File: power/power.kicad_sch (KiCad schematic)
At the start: 160 parts, among them J1 USB-C Power + USB2.0, J2 USB, J3 BATTERY OUT, J4 BACKUP, Q1 SI7617DN-T1-GE3, Q2 CSD18534Q5A, Q3 CSD18534Q5A, Q4 CSD18534Q5A, Q5 CSD18534Q5A, Q6 CSD18534Q5A, Q7 CSD18534Q5A, Q8 CSD18534Q5A, SW1 RST, SW2 BOOT, U1 HUSB238, U2 LTC2943, U3 BQ7791501PWR, U4 BQ25713RSNR, U5 ESP32-S3-MINI-1, U6 TVS2200DRV, U7 TPS560200, U8 CP2102N-Axx-xQFN28

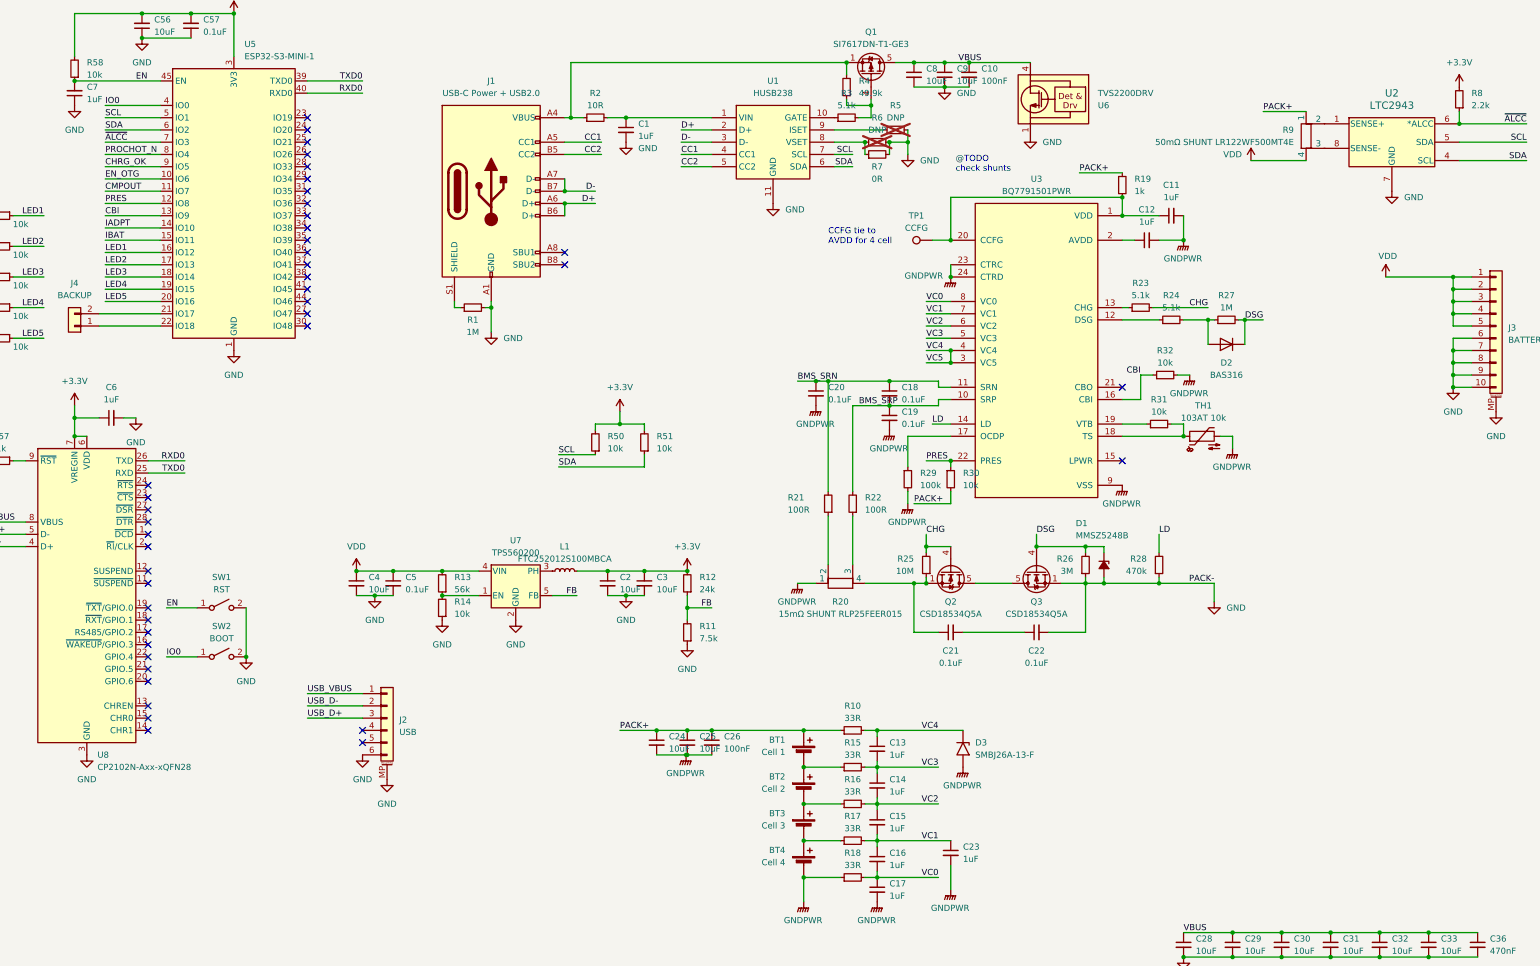
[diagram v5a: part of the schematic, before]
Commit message: silkscreening power
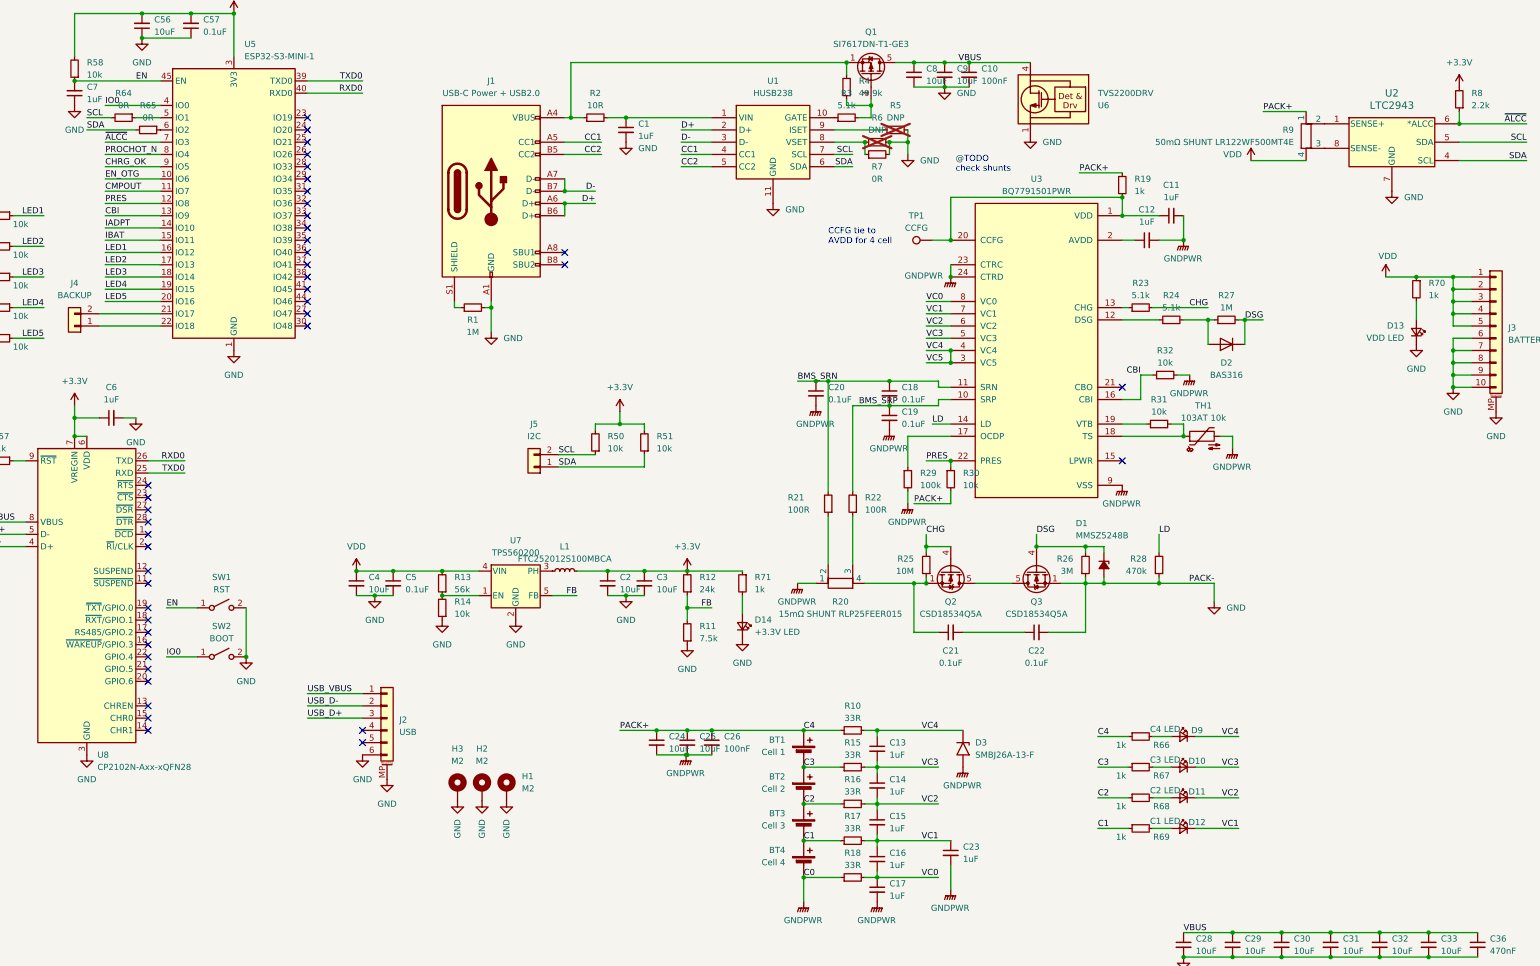
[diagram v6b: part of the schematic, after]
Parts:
- added D10: C3 LED, LED_SMD:LED_0603_1608Metric, symbol Device:LED_Small
- added D11: C2 LED, LED_SMD:LED_0603_1608Metric, symbol Device:LED_Small
- added D12: C1 LED, LED_SMD:LED_0603_1608Metric, symbol Device:LED_Small
- added D13: VDD LED, LED_SMD:LED_0603_1608Metric, symbol Device:LED_Small
- added D14: +3.3V LED, LED_SMD:LED_0603_1608Metric, symbol Device:LED_Small
- added D9: C4 LED, LED_SMD:LED_0603_1608Metric, symbol Device:LED_Small
- added H1, H2, H3: M2, MountingHole:MountingHole_2.2mm_M2_Pad_Via, symbol Mechanical:MountingHole_Pad
- added J5: I2C, Connector_PinHeader_2.54mm:PinHeader_1x02_P2.54mm_Vertical, symbol Connector_Generic:Conn_01x02
- added R64, R65: 0R, Resistor_SMD:R_0603_1608Metric, symbol Device:R_Small
- added R66, R67, R68, R69, R70, R71: 1k, Resistor_SMD:R_0603_1608Metric, symbol Device:R_Small
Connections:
- net +3.3V: now also R71.1
- net GND: now also D13.1 (K), D14.1 (K), H1.1, H2.1, H3.1
- net SCL: now also J5.2 (Pin_2), R64.2; no longer U5.5 (IO1)
- net SDA: now also J5.1 (Pin_1), R65.2; no longer U5.6 (IO2)
- net VC1: now also D12.1 (K)
- net VC2: now also D11.1 (K)
- net VC3: now also D10.1 (K)
- net VC4: now also D9.1 (K)
- net VDD: now also R70.1
- net C1: now reaches BT3.2 (-), BT4.1 (+), R17.1
- net C1: now also R69.1
- net C2: now reaches BT2.2 (-), BT3.1 (+), R16.1
- net C2: now also R68.1
- net C3: now reaches BT1.2 (-), BT2.1 (+), R15.1
- net C3: now also R67.1
- net PACK+ renamed C4
- net C4: now also R66.1
- new net: D13.2 (A), R70.2
- new net: D9.2 (A), R66.2
- new net: D11.2 (A), R68.2
- new net: D12.2 (A), R69.2
- new net: D10.2 (A), R67.2
- new net: R64.1, U5.5 (IO1)
- new net: R65.1, U5.6 (IO2)
- new net: D14.2 (A), R71.2
